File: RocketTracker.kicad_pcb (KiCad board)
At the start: 2 copper layers, 36 parts, among them J1 HW_SERIAL, J10 ANT, J2 GPS_SERIAL, J3 LAUNCH1, J4 LAUNCH2, J5 I2C_PRESSURE, J6 SD_Card, J7 PWR_IN, J8 I2C_GYRO, J9 I2C_RTC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

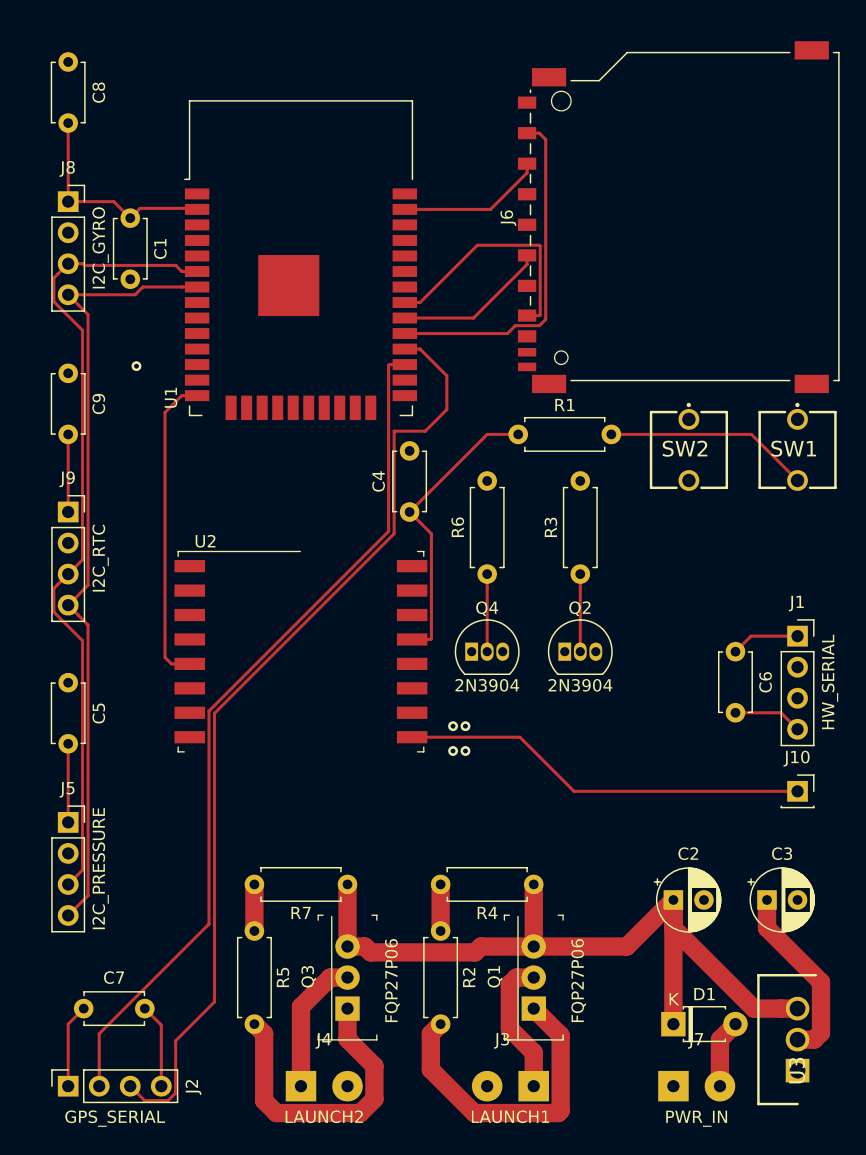
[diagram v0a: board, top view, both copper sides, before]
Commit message: Use smaller components
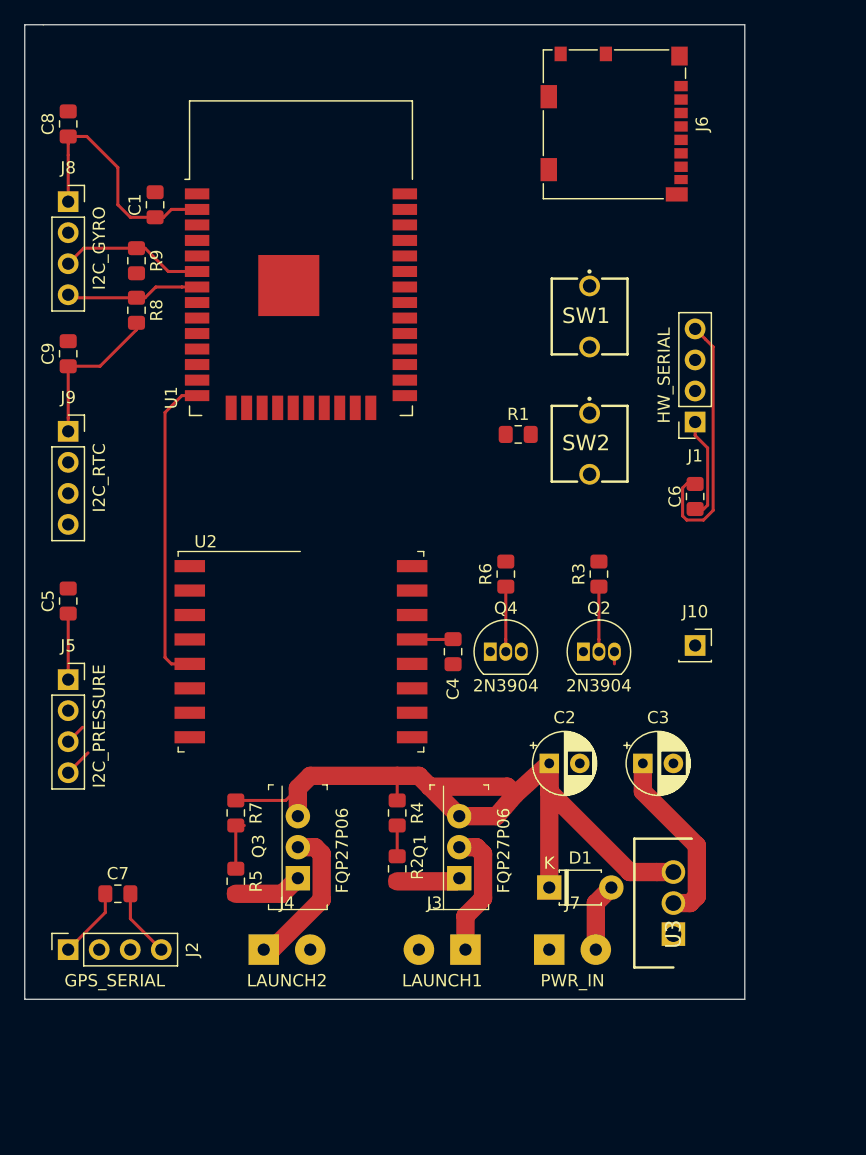
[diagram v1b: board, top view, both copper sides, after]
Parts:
- added R8: 4K7, Resistor_SMD:R_0805_2012Metric_Pad1.15x1.40mm_HandSolder, F.Cu at (104.6, 76.2)
- added R9: 4K7, Resistor_SMD:R_0805_2012Metric_Pad1.15x1.40mm_HandSolder, F.Cu at (104.6, 72.1)
- C1, C4, C5, C6, C7, C8, C9: footprint Capacitor_THT:C_Disc_D4.7mm_W2.5mm_P5.00mm -> Capacitor_SMD:C_0805_2012Metric_Pad1.15x1.40mm_HandSolder
- J6: value SD_Card -> Micro_SD_Card; footprint Connector_Card:SD_TE_2041021 -> Connector_Card:microSD_HC_Molex_104031-0811
- R1, R2, R3, R4, R5, R6, R7: footprint Resistor_THT:R_Axial_DIN0207_L6.3mm_D2.5mm_P7.62mm_Horizontal -> Resistor_SMD:R_0805_2012Metric_Pad1.15x1.40mm_HandSolder
- moved SW1 20.2 mm to (141.7, 76.7)
- moved J1 19.4 mm to (150.4, 85.3), turned to 180 degrees
- moved D1 15.1 mm to (138.4, 123.4)
- moved U3 15.1 mm to (148.6, 127.3)
- moved C2 15.1 mm to (138.4, 113.3)
- moved C3 15.1 mm to (146.1, 113.3)
- moved J7 15.1 mm to (138.4, 128.5)
- moved J10 14.6 mm to (150.4, 103.6)
- moved C6 13.1 mm to (150.4, 91.4), turned to 90 degrees
- moved R4 12.6 mm to (126.0, 117.3), turned to 270 degrees
- moved J3 12.5 mm to (131.6, 128.5)
- moved Q1 12.3 mm to (131.1, 122.7)
- moved C4 12.0 mm to (130.6, 104.1), turned to 270 degrees
- moved C5 11.7 mm to (99.1, 100.0)
- moved J5 11.7 mm to (99.1, 106.4)
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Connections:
- J6 pad 1: CS0 -> (no net)
- J6 pad 2: MOSI -> CS0
- J6 pad 3: GND -> MOSI
- J6 pad 6: GND -> +3V3
- J6 pad 9: (no net) -> GND
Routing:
- net GPSRX: track 78.2 -> 0.00 mm
- net GPSTX: track 70.1 -> 0.00 mm
- net SCL: track 65.5 -> 13.5 mm
- net SDA: track 64.3 -> 13.3 mm
- net Net-(J10-Pad1): track 33.4 -> 0.00 mm
- net CS0: track 28.5 -> 0.00 mm
- net Net-(Q1-Pad1): track 25.5 -> 5.19 mm
- net MISO: track 19.8 -> 0.00 mm
- net Net-(Q3-Pad1): track 24.8 -> 5.61 mm
- net Net-(R1-Pad2): track 16.8 -> 0.00 mm
- net GND: track 12.5 -> 27.5 mm
- net CLK: track 12.6 -> 0.00 mm
- net MOSI: track 12.0 -> 0.00 mm
- net +3V3: track 82.2 -> 71.3 mm
- net +BATT: track 64.2 -> 66.6 mm
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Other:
- board outline added: 58.9 x 79.8 mm

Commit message: Connect up traces
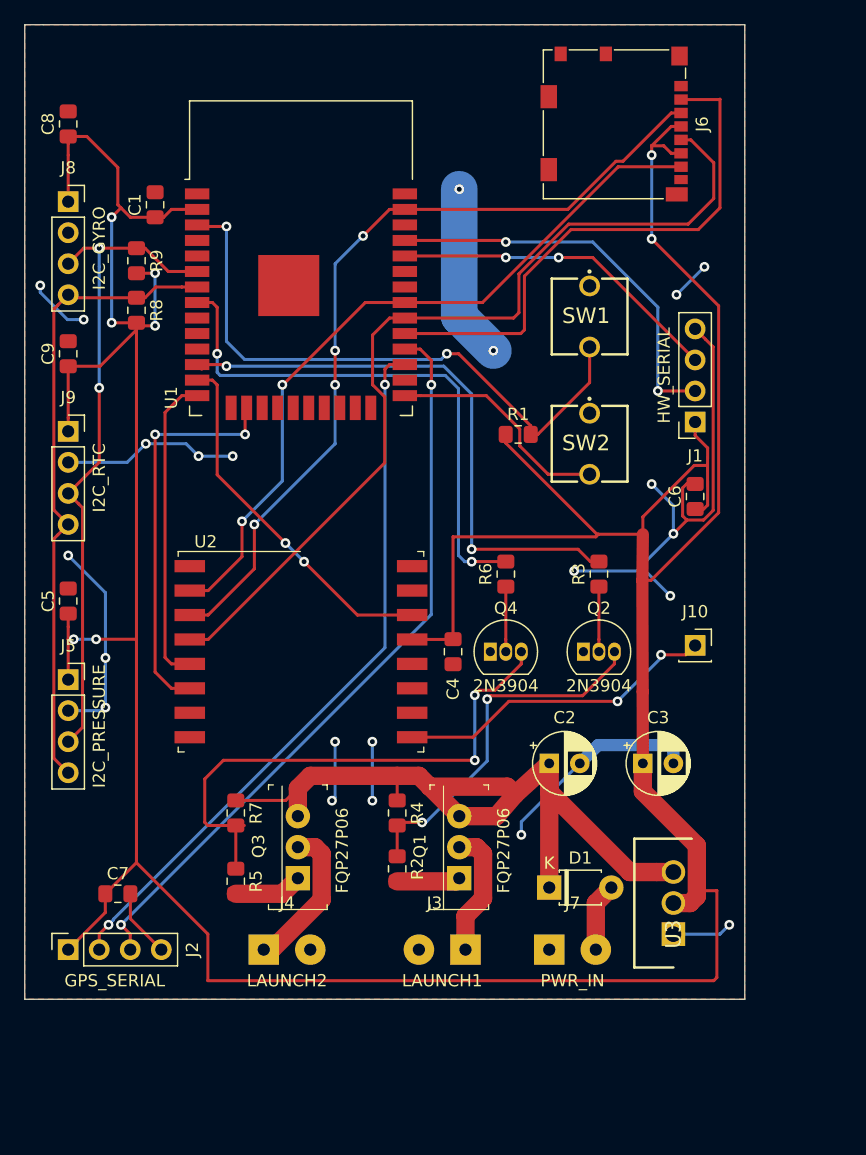
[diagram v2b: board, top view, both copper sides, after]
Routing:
- net +3V3: track 71.3 -> 316.6 mm, vias 0 -> 8
- net GND: track 27.5 -> 132.6 mm, vias 0 -> 22
- net CLK: track 0.00 -> 73.6 mm
- net MOSI: track 0.00 -> 68.0 mm, vias 0 -> 4
- net GPSRX: track 0.00 -> 61.6 mm, vias 0 -> 2
- net MISO: track 0.00 -> 60.9 mm, vias 0 -> 2
- net GPSTX: track 0.00 -> 59.0 mm, vias 0 -> 2
- net Net-(R1-Pad2): track 0.00 -> 50.2 mm, vias 0 -> 2
- net LAUNCH1: track 0.00 -> 47.5 mm, vias 0 -> 2
- net LAUNCH2: track 0.00 -> 45.3 mm, vias 0 -> 2
- net CS0: track 0.00 -> 44.7 mm
- net SCL: track 13.5 -> 54.3 mm, vias 0 -> 2
- net Net-(Q4-Pad3): track 4.24 -> 44.4 mm, vias 0 -> 2
- net SDA: track 13.3 -> 52.1 mm
- net HW_TX: track 0.00 -> 32.9 mm, vias 0 -> 2
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- added copper zone on F.Cu, net GND

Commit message: Add updated board
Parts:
- added REF**: OSHW-Logo2_7.3x6mm_SilkScreen, Symbol:OSHW-Logo2_7.3x6mm_SilkScreen, F.Cu at (104.9, 117.7)
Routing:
- net GND: track 132.6 -> 171.1 mm, vias 22 -> 26
- net +3V3: track 316.6 -> 307.3 mm
- net Net-(SW2-Pad2): track 18.6 -> 21.0 mm, vias 0 -> 2
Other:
- outline, holes or cut-outs redrawn
- rule trace_min: 0.2 -> 0.25
- board text added: "+"
- board text added: "-"
- board text added: "CONNECT ANTENNA BEFORE TX!"
- board text added: "HARWELL ROCKET CLUB TRACKER V1"
- board text added: "L"
- board text added: "SCL"
- board text added: "SDA"
- board text added: "Will Furnell 2020"
- board text added: "hello"
